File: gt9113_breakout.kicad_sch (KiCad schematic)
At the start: 12 parts, among them J1 Conn_01x09_Male, J7 504740-5100, J8 504740-5100, U1 GT9113

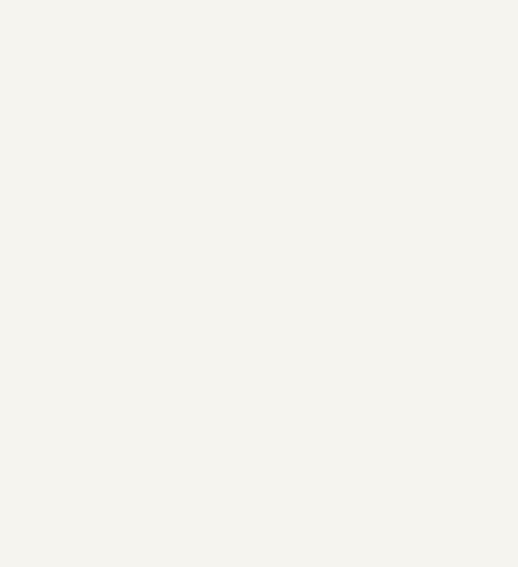
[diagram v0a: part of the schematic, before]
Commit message: refactor gt9113_breakout into hierarchical sheet.
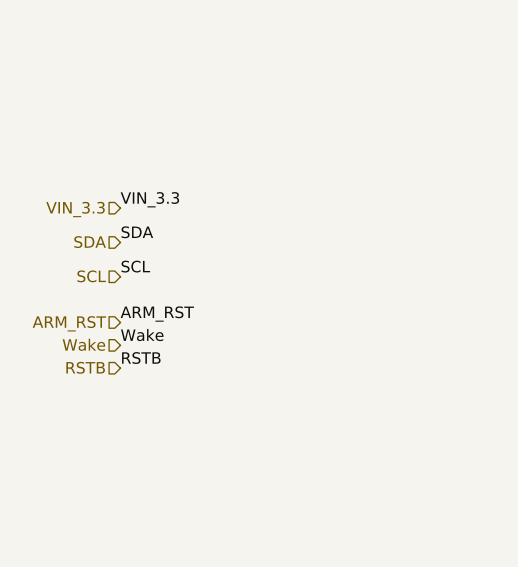
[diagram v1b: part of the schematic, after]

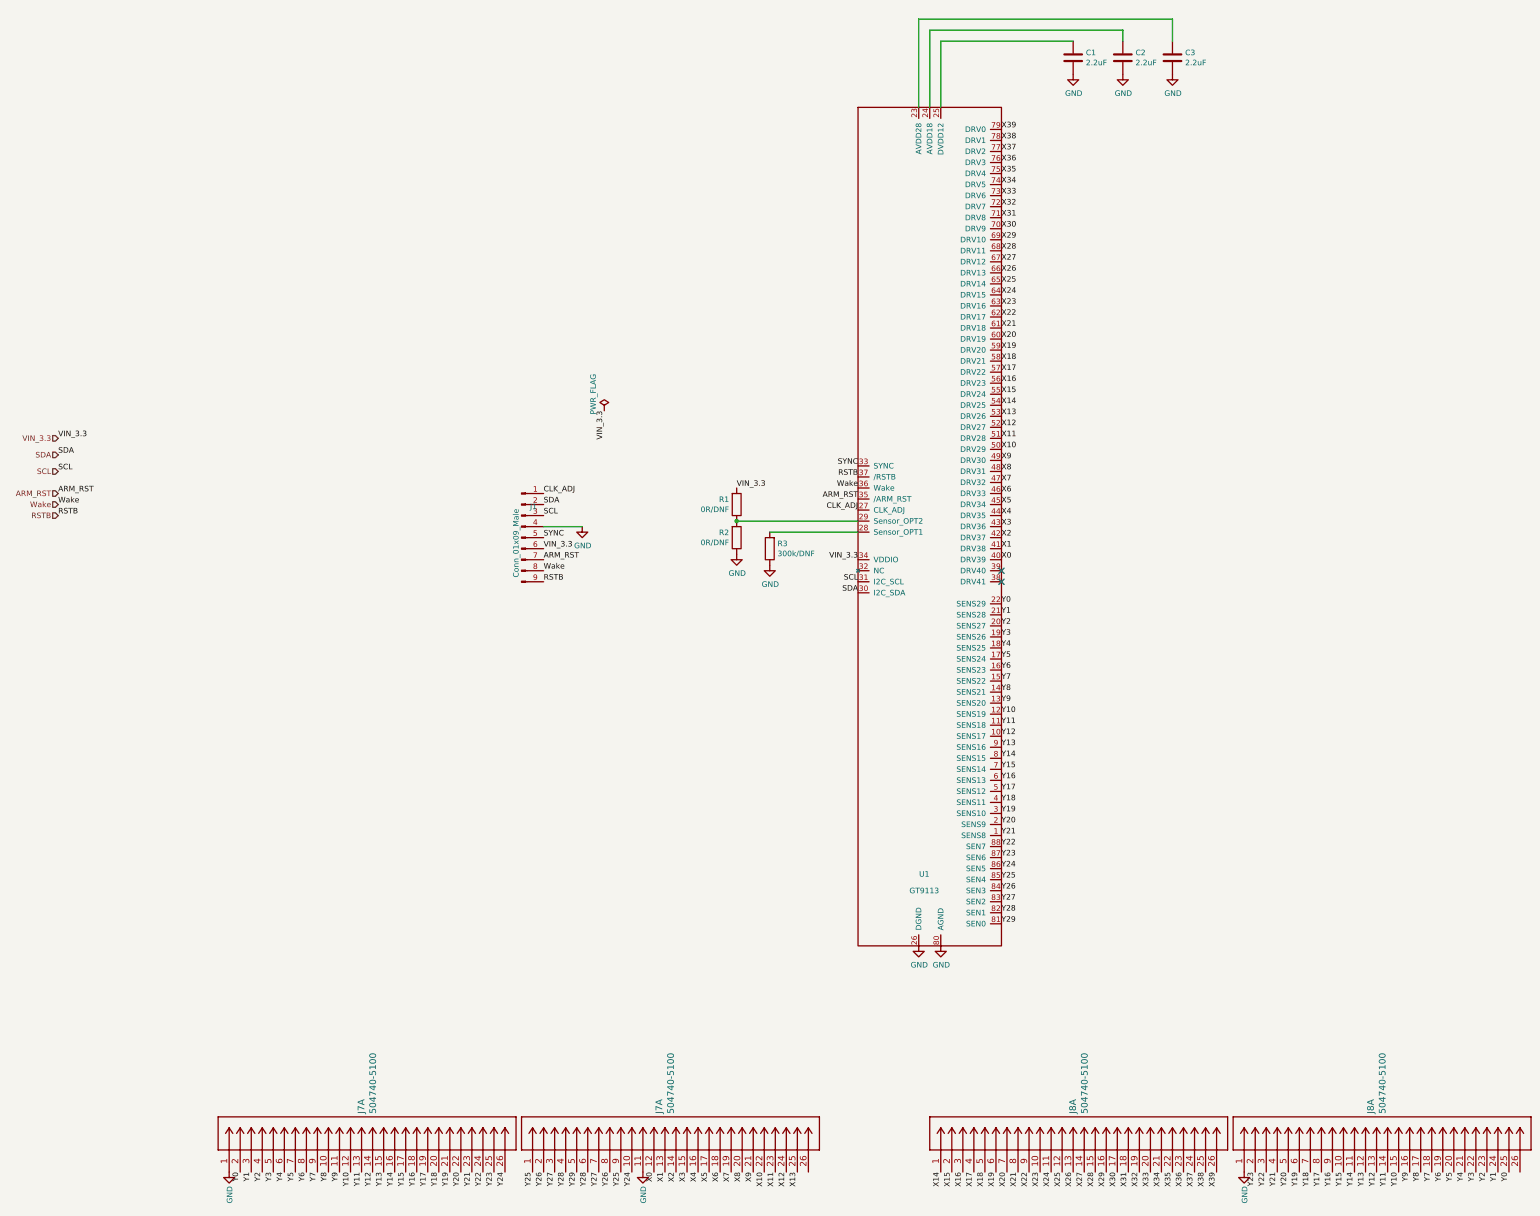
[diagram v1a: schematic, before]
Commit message: Merge gt9113_breakout.kicad_pcb into pipad.kicad_pcb
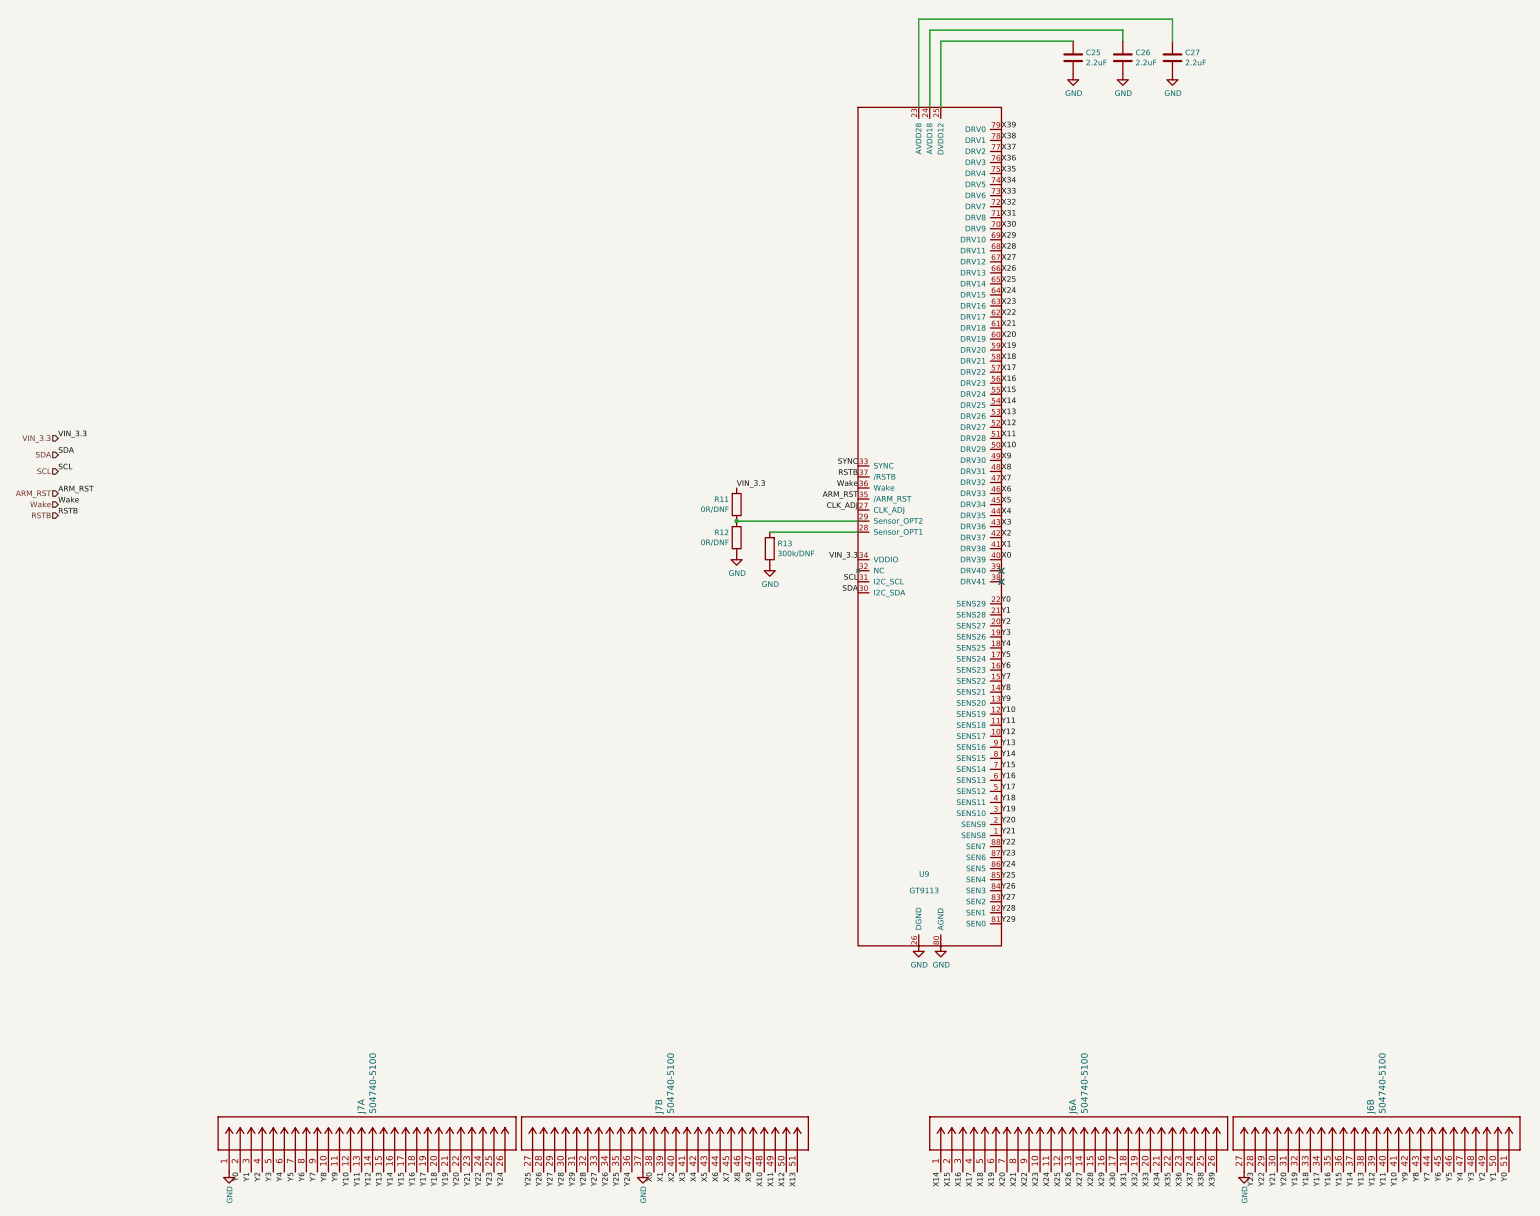
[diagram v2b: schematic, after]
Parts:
- removed J1: Conn_01x09_Male, Connector_PinHeader_2.54mm:PinHeader_1x09_P2.54mm_Vertical, symbol Connector:Conn_01x09_Male
- renumbered C1 to C25, C2 to C26, C3 to C27, J8 to J6, R1 to R11, R2 to R12, R3 to R13, U1 to U9
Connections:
- net GND: now also J6.27, J7.37; no longer J6.1, J7.11
- net X0: now also J7.38; no longer J7.12
- net X1: now also J7.39; no longer J7.13
- net X10: now also J7.48; no longer J7.22
- net X11: now also J7.49; no longer J7.23
- net X12: now also J7.50; no longer J7.24
- net X13: now also J7.51; no longer J7.25
- net X2: now also J7.40; no longer J7.14
- net X3: now also J7.41; no longer J7.15
- net X4: now also J7.42; no longer J7.16
- net X5: now also J7.43; no longer J7.17
- net X6: now also J7.44; no longer J7.18
- net X7: now also J7.45; no longer J7.19
- net X8: now also J7.46; no longer J7.20
- net X9: now also J7.47; no longer J7.21
- net Y0: now also J6.51; no longer J6.25
- net Y1: now also J6.50; no longer J6.24
- net Y10: now also J6.41; no longer J6.15
- net Y11: now also J6.40; no longer J6.14
- net Y12: now also J6.39; no longer J6.13
- net Y13: now also J6.38; no longer J6.12
- net Y14: now also J6.37; no longer J6.11
- net Y15: now also J6.36; no longer J6.10
- net Y16: now also J6.35; no longer J6.9
- net Y17: now also J6.34; no longer J6.8
- net Y18: now also J6.33; no longer J6.7
- net Y19: now also J6.32; no longer J6.6
- net Y2: now also J6.49; no longer J6.23
- net Y20: now also J6.31; no longer J6.5
- net Y21: now also J6.30; no longer J6.4
- net Y22: now also J6.29; no longer J6.3
- net Y23: now also J6.28; no longer J6.2
- net Y24: now also J7.36; no longer J7.10
- net Y25: now also J7.27, J7.35; no longer J7.1, J7.9
- net Y26: now also J7.28, J7.34; no longer J7.2, J7.8
- net Y27: now also J7.29, J7.33; no longer J7.3, J7.7
- net Y28: now also J7.30, J7.32; no longer J7.4, J7.6
- net Y29: now also J7.31; no longer J7.5
- net Y3: now also J6.48; no longer J6.22
- net Y4: now also J6.47; no longer J6.21
- net Y5: now also J6.46; no longer J6.20
- net Y6: now also J6.45; no longer J6.19
- net Y7: now also J6.44; no longer J6.18
- net Y8: now also J6.43; no longer J6.17
- net Y9: now also J6.42; no longer J6.16

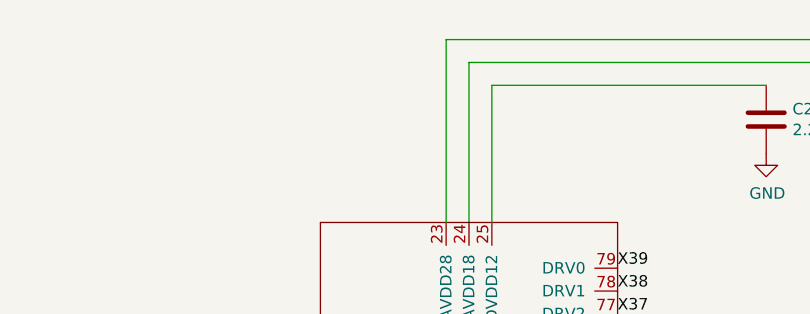
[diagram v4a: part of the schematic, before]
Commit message: Fix (or ignore) all ERC and DRC errors.
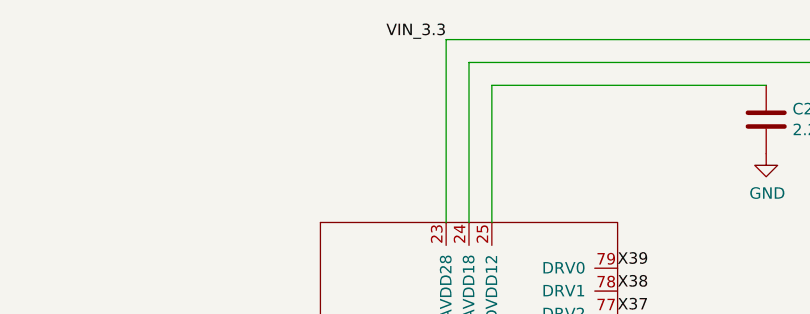
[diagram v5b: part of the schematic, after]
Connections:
- net VIN_3.3: now also C27.1, U9.23 (AVDD28)
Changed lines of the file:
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@@
+    (effects (font (size 1.27 1.27)) (justify right bottom))
+  )
+  (label "VIN_3.3" (at 247.65 24.13 180)
     (effects (font (size 1.27 1.27)) (justify right bottom))
   )

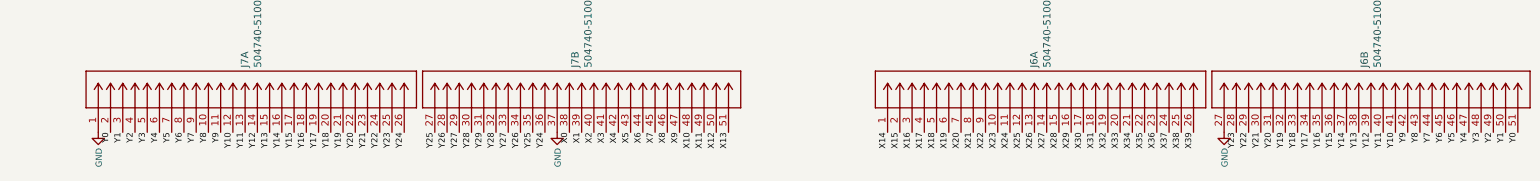
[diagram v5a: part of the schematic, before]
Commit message: WIP: Flip the touchscreen connectors. Fixes #2.
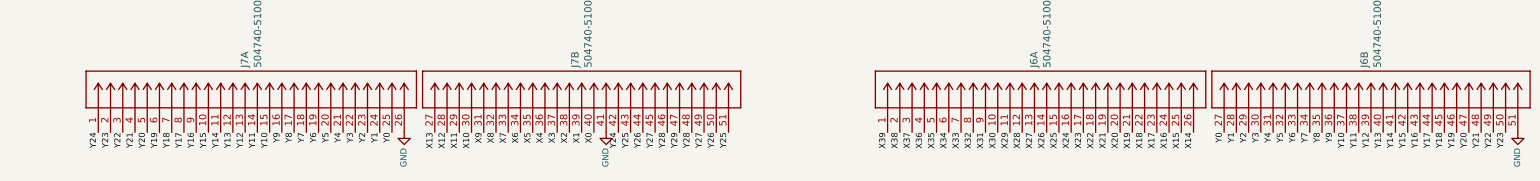
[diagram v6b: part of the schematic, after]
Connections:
- net GND: now also J6.51, J7.26, J7.41; no longer J6.27, J7.1, J7.37
- net X0: now also J7.40; no longer J7.38
- net X10: now also J7.30; no longer J7.48
- net X11: now also J7.29; no longer J7.49
- net X12: now also J7.28; no longer J7.50
- net X13: now also J7.27; no longer J7.51
- net X14: now also J6.26; no longer J6.1
- net X15: now also J6.25; no longer J6.2
- net X16: now also J6.24; no longer J6.3
- net X17: now also J6.23; no longer J6.4
- net X18: now also J6.22; no longer J6.5
- net X19: now also J6.21; no longer J6.6
- net X2: now also J7.38; no longer J7.40
- net X20: now also J6.20; no longer J6.7
- net X21: now also J6.19; no longer J6.8
- net X22: now also J6.18; no longer J6.9
- net X23: now also J6.17; no longer J6.10
- net X24: now also J6.16; no longer J6.11
- net X25: now also J6.15; no longer J6.12
- net X26: now also J6.14; no longer J6.13
- net X27: now also J6.13; no longer J6.14
- net X28: now also J6.12; no longer J6.15
- net X29: now also J6.11; no longer J6.16
- net X3: now also J7.37; no longer J7.41
- net X30: now also J6.10; no longer J6.17
- net X31: now also J6.9; no longer J6.18
- net X32: now also J6.8; no longer J6.19
- net X33: now also J6.7; no longer J6.20
- net X34: now also J6.6; no longer J6.21
- net X35: now also J6.5; no longer J6.22
- net X36: now also J6.4; no longer J6.23
- net X37: now also J6.3; no longer J6.24
- net X38: now also J6.2; no longer J6.25
- net X39: now also J6.1; no longer J6.26
- net X4: now also J7.36; no longer J7.42
- net X5: now also J7.35; no longer J7.43
- net X6: now also J7.34; no longer J7.44
- net X7: now also J7.33; no longer J7.45
- net X8: now also J7.32; no longer J7.46
- net X9: now also J7.31; no longer J7.47
- net Y0: now also J6.27, J7.25; no longer J6.51, J7.2
- net Y1: now also J6.28, J7.24; no longer J6.50, J7.3
- net Y10: now also J6.37, J7.15; no longer J6.41, J7.12
- net Y11: now also J6.38, J7.14; no longer J6.40, J7.13
- net Y12: now also J7.13; no longer J7.14
- net Y13: now also J6.40, J7.12; no longer J6.38, J7.15
- net Y14: now also J6.41, J7.11; no longer J6.37, J7.16
- net Y15: now also J6.42, J7.10; no longer J6.36, J7.17
- net Y16: now also J6.43, J7.9; no longer J6.35, J7.18
- net Y17: now also J6.44, J7.8; no longer J6.34, J7.19
- net Y18: now also J6.45, J7.7; no longer J6.33, J7.20
- net Y19: now also J6.46, J7.6; no longer J6.32, J7.21
- net Y2: now also J6.29, J7.23; no longer J6.49, J7.4
- net Y20: now also J6.47, J7.5; no longer J6.31, J7.22
- net Y21: now also J6.48, J7.4; no longer J6.30, J7.23
- net Y22: now also J6.49, J7.3; no longer J6.29, J7.24
- net Y23: now also J6.50, J7.2; no longer J6.28, J7.25
- net Y24: now also J7.1, J7.42; no longer J7.26, J7.36
- net Y25: now also J7.43, J7.51; no longer J7.27, J7.35
- net Y26: now also J7.44, J7.50; no longer J7.28, J7.34
- net Y27: now also J7.45, J7.49; no longer J7.29, J7.33
- net Y28: now also J7.46, J7.48; no longer J7.30, J7.32
- net Y29: now also J7.47; no longer J7.31
- net Y3: now also J6.30, J7.22; no longer J6.48, J7.5
- net Y4: now also J6.31, J7.21; no longer J6.47, J7.6
- net Y5: now also J6.32, J7.20; no longer J6.46, J7.7
- net Y6: now also J6.33, J7.19; no longer J6.45, J7.8
- net Y7: now also J6.34, J7.18; no longer J6.44, J7.9
- net Y8: now also J6.35, J7.17; no longer J6.43, J7.10
- net Y9: now also J6.36, J7.16; no longer J6.42, J7.11

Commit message: Route DSI signals. Also fix the schematic for the touchscreen connectors, which got messed up somehow.
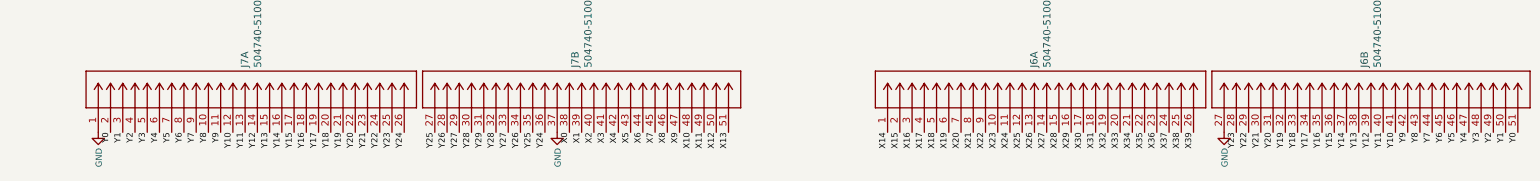
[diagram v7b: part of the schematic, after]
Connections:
- net GND: now also J6.27, J7.1, J7.37; no longer J6.51, J7.26, J7.41
- net X0: now also J7.38; no longer J7.40
- net X10: now also J7.48; no longer J7.30
- net X11: now also J7.49; no longer J7.29
- net X12: now also J7.50; no longer J7.28
- net X13: now also J7.51; no longer J7.27
- net X14: now also J6.1; no longer J6.26
- net X15: now also J6.2; no longer J6.25
- net X16: now also J6.3; no longer J6.24
- net X17: now also J6.4; no longer J6.23
- net X18: now also J6.5; no longer J6.22
- net X19: now also J6.6; no longer J6.21
- net X2: now also J7.40; no longer J7.38
- net X20: now also J6.7; no longer J6.20
- net X21: now also J6.8; no longer J6.19
- net X22: now also J6.9; no longer J6.18
- net X23: now also J6.10; no longer J6.17
- net X24: now also J6.11; no longer J6.16
- net X25: now also J6.12; no longer J6.15
- net X26: now also J6.13; no longer J6.14
- net X27: now also J6.14; no longer J6.13
- net X28: now also J6.15; no longer J6.12
- net X29: now also J6.16; no longer J6.11
- net X3: now also J7.41; no longer J7.37
- net X30: now also J6.17; no longer J6.10
- net X31: now also J6.18; no longer J6.9
- net X32: now also J6.19; no longer J6.8
- net X33: now also J6.20; no longer J6.7
- net X34: now also J6.21; no longer J6.6
- net X35: now also J6.22; no longer J6.5
- net X36: now also J6.23; no longer J6.4
- net X37: now also J6.24; no longer J6.3
- net X38: now also J6.25; no longer J6.2
- net X39: now also J6.26; no longer J6.1
- net X4: now also J7.42; no longer J7.36
- net X5: now also J7.43; no longer J7.35
- net X6: now also J7.44; no longer J7.34
- net X7: now also J7.45; no longer J7.33
- net X8: now also J7.46; no longer J7.32
- net X9: now also J7.47; no longer J7.31
- net Y0: now also J6.51, J7.2; no longer J6.27, J7.25
- net Y1: now also J6.50, J7.3; no longer J6.28, J7.24
- net Y10: now also J6.41, J7.12; no longer J6.37, J7.15
- net Y11: now also J6.40, J7.13; no longer J6.38, J7.14
- net Y12: now also J7.14; no longer J7.13
- net Y13: now also J6.38, J7.15; no longer J6.40, J7.12
- net Y14: now also J6.37, J7.16; no longer J6.41, J7.11
- net Y15: now also J6.36, J7.17; no longer J6.42, J7.10
- net Y16: now also J6.35, J7.18; no longer J6.43, J7.9
- net Y17: now also J6.34, J7.19; no longer J6.44, J7.8
- net Y18: now also J6.33, J7.20; no longer J6.45, J7.7
- net Y19: now also J6.32, J7.21; no longer J6.46, J7.6
- net Y2: now also J6.49, J7.4; no longer J6.29, J7.23
- net Y20: now also J6.31, J7.22; no longer J6.47, J7.5
- net Y21: now also J6.30, J7.23; no longer J6.48, J7.4
- net Y22: now also J6.29, J7.24; no longer J6.49, J7.3
- net Y23: now also J6.28, J7.25; no longer J6.50, J7.2
- net Y24: now also J7.26, J7.36; no longer J7.1, J7.42
- net Y25: now also J7.27, J7.35; no longer J7.43, J7.51
- net Y26: now also J7.28, J7.34; no longer J7.44, J7.50
- net Y27: now also J7.29, J7.33; no longer J7.45, J7.49
- net Y28: now also J7.30, J7.32; no longer J7.46, J7.48
- net Y29: now also J7.31; no longer J7.47
- net Y3: now also J6.48, J7.5; no longer J6.30, J7.22
- net Y4: now also J6.47, J7.6; no longer J6.31, J7.21
- net Y5: now also J6.46, J7.7; no longer J6.32, J7.20
- net Y6: now also J6.45, J7.8; no longer J6.33, J7.19
- net Y7: now also J6.44, J7.9; no longer J6.34, J7.18
- net Y8: now also J6.43, J7.10; no longer J6.35, J7.17
- net Y9: now also J6.42, J7.11; no longer J6.36, J7.16
